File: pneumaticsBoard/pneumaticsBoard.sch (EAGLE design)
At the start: 51 parts, among them IC1 MAX232, Q1 60V/32A/35mΩ, Q2 60V/32A/35mΩ, Q3 60V/32A/35mΩ, Q4 60V/32A/35mΩ, Q5 60V/32A/35mΩ, Q6 60V/32A/35mΩ, Q7 60V/32A/35mΩ, Q8 60V/32A/35mΩ, U1 ATMEGA328P-PU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

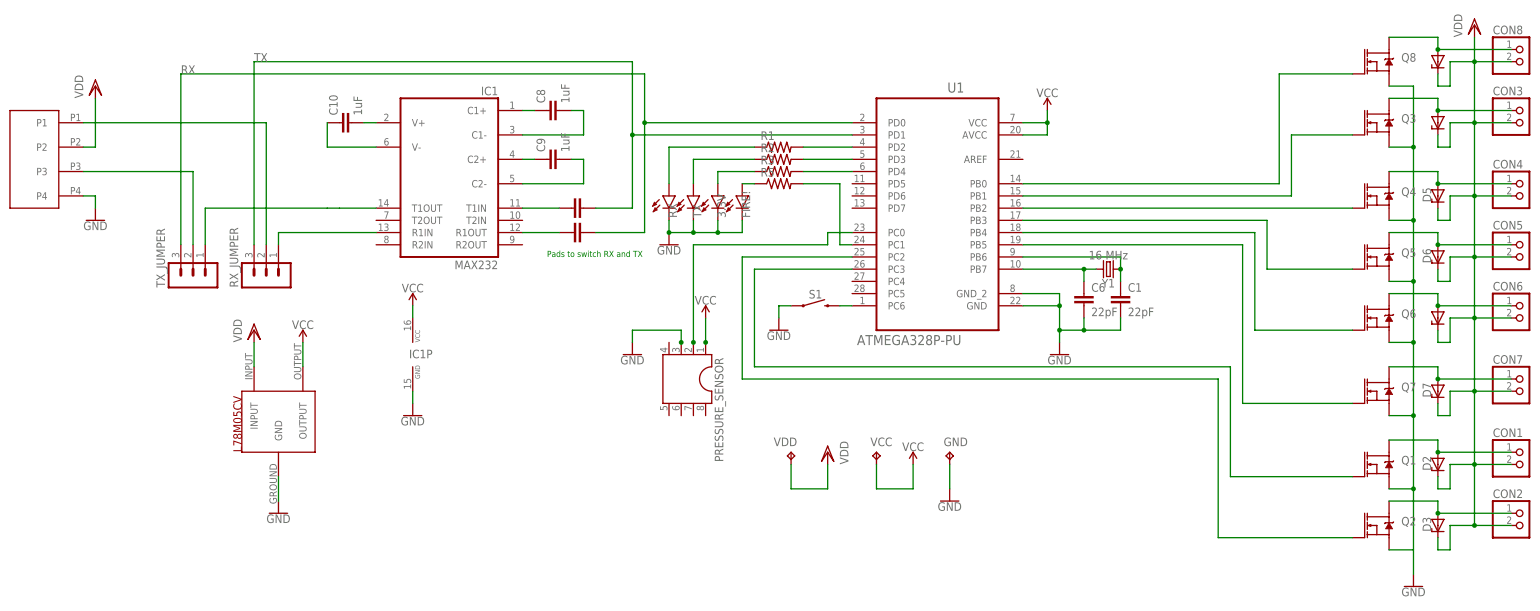
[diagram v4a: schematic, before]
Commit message: Changed regulator position, fixed traces
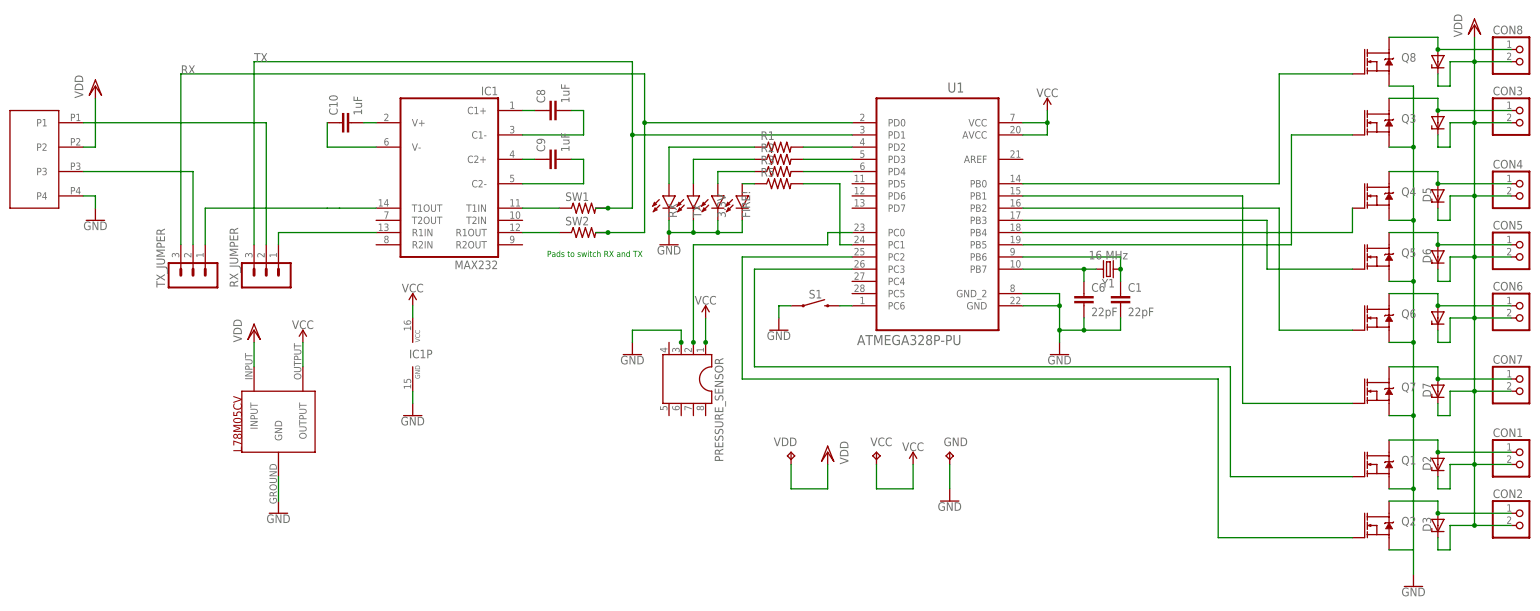
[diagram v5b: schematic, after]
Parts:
- removed C2, C3: 1uF, SparkFun-Capacitors:470PF-0603-50V-5%
- added SW1, SW2: (no value), resistor:R-US_0204/2V
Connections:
- removed net Q4: Q4.G, U1.PB2
- new net N$5: Q4.G, U1.PB4
- net N$17: now also SW1.1; no longer C2.1
- net N$18: now also SW2.1; no longer C3.1
- net Q3: now also U1.PB5; no longer U1.PB1
- net Q6: now also U1.PB2; no longer U1.PB4
- net Q7: now also U1.PB1; no longer U1.PB5
- net RX: now also SW2.2; no longer C3.2
- net TX: now also SW1.2; no longer C2.2
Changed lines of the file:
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@@
 <part name="TX_JUMPER" library="con-lstb" library_urn="urn:adsk.eagle:library:162" deviceset="MA03-1" device="" package3d_urn="urn:adsk.eagle:package:8339/1"/>
 <part name="RX_JUMPER" library="con-lstb" library_urn="urn:adsk.eagle:library:162" deviceset="MA03-1" device="" package3d_urn="urn:adsk.eagle:package:8339/1"/>
-<part name="C2" library="SparkFun-Capacitors" deviceset="470PF" device="-0603-50V-5%" value="1uF"/>
-<part name="C3" library="SparkFun-Capacitors" deviceset="470PF" device="-0603-50V-5%" value="1uF"/>
 <part name="Q1" library="SparkFun-DiscreteSemi" deviceset="MOSFET-NCH" device="-FQP30N06L" value="60V/32A/35mΩ"/>
 <part name="Q2" library="SparkFun-DiscreteSemi" deviceset="MOSFET-NCH" device="-FQP30N06L" value="60V/32A/35mΩ"/>
@@
 <part name="SUPPLY3" library="SparkFun-PowerSymbols" deviceset="VCC" device=""/>
 <part name="GND4" library="SparkFun-PowerSymbols" deviceset="GND" device=""/>
+<part name="SW2" library="resistor" library_urn="urn:adsk.eagle:library:348" deviceset="R-US_" device="0204/2V" package3d_urn="urn:adsk.eagle:package:25948/1"/>
+<part name="SW1" library="resistor" library_urn="urn:adsk.eagle:library:348" deviceset="R-US_" device="0204/2V" package3d_urn="urn:adsk.eagle:package:25948/1"/>
 </parts>
 <sheets>
@@
 <instance part="TX_JUMPER" gate="G$1" x="-137.16" y="25.4" rot="R90"/>
 <instance part="RX_JUMPER" gate="G$1" x="-121.92" y="25.4" rot="R90"/>
-<instance part="C2" gate="G$1" x="-55.88" y="40.64" smashed="yes" rot="R90"/>
-<instance part="C3" gate="G$1" x="-55.88" y="35.56" smashed="yes" rot="R90"/>
 <instance part="Q1" gate="NMOS" x="109.22" y="-12.7" smashed="yes">
 <attribute name="NAME" x="114.3" y="-12.7" size="1.778" layer="95" font="vector"/>
@@
 <instance part="SUPPLY3" gate="G$1" x="-114.3" y="12.7" rot="MR0"/>
 <instance part="GND4" gate="1" x="-119.38" y="-22.86"/>
+<instance part="SW2" gate="G$1" x="-55.88" y="35.56"/>
+<instance part="SW1" gate="G$1" x="-55.88" y="40.64"/>
 </instances>
 <busses>
@@
 <net name="Q3" class="0">
 <segment>
-<wire x1="91.44" y1="55.88" x2="91.44" y2="43.18" width="0.1524" layer="91"/>
+<wire x1="91.44" y1="55.88" x2="91.44" y2="33.02" width="0.1524" layer="91"/>
 <wire x1="104.14" y1="55.88" x2="91.44" y2="55.88" width="0.1524" layer="91"/>
-<pinref part="U1" gate="A" pin="PB1"/>
-<wire x1="91.44" y1="43.18" x2="35.56" y2="43.18" width="0.1524" layer="91"/>
 <pinref part="Q3" gate="NMOS" pin="G"/>
-</segment>
-</net>
-<net name="Q4" class="0">
-<segment>
-<wire x1="104.14" y1="40.64" x2="35.56" y2="40.64" width="0.1524" layer="91"/>
-<pinref part="U1" gate="A" pin="PB2"/>
-<pinref part="Q4" gate="NMOS" pin="G"/>
+<pinref part="U1" gate="A" pin="PB5"/>
+<wire x1="35.56" y1="33.02" x2="91.44" y2="33.02" width="0.1524" layer="91"/>
 </segment>
 </net>
@@
 <wire x1="86.36" y1="27.94" x2="86.36" y2="38.1" width="0.1524" layer="91"/>
 <wire x1="104.14" y1="27.94" x2="86.36" y2="27.94" width="0.1524" layer="91"/>
+<pinref part="Q5" gate="NMOS" pin="G"/>
 <pinref part="U1" gate="A" pin="PB3"/>
 <wire x1="35.56" y1="38.1" x2="86.36" y2="38.1" width="0.1524" layer="91"/>
-<pinref part="Q5" gate="NMOS" pin="G"/>
 </segment>
 </net>
@@
 <wire x1="-43.18" y1="58.42" x2="-43.18" y2="35.56" width="0.1524" layer="91"/>
 <pinref part="U1" gate="A" pin="PD0"/>
-<wire x1="-53.34" y1="35.56" x2="-43.18" y2="35.56" width="0.1524" layer="91"/>
+<wire x1="-53.34" y1="35.56" x2="-50.8" y2="35.56" width="0.1524" layer="91"/>
+<wire x1="-50.8" y1="35.56" x2="-43.18" y2="35.56" width="0.1524" layer="91"/>
 <wire x1="0" y1="58.42" x2="-43.18" y2="58.42" width="0.1524" layer="91"/>
 <wire x1="-43.18" y1="68.58" x2="-43.18" y2="58.42" width="0.1524" layer="91"/>
@@
 <wire x1="-43.18" y1="68.58" x2="-139.7" y2="68.58" width="0.1524" layer="91"/>
 <label x="-139.7" y="68.58" size="1.778" layer="95"/>
-<pinref part="C3" gate="G$1" pin="2"/>
+<pinref part="SW2" gate="G$1" pin="2"/>
+<junction x="-50.8" y="35.56"/>
 </segment>
 </net>
@@
 <net name="Q7" class="0">
 <segment>
-<pinref part="U1" gate="A" pin="PB5"/>
 <wire x1="104.14" y1="0" x2="81.28" y2="0" width="0.1524" layer="91"/>
-<wire x1="81.28" y1="0" x2="81.28" y2="33.02" width="0.1524" layer="91"/>
-<wire x1="35.56" y1="33.02" x2="81.28" y2="33.02" width="0.1524" layer="91"/>
+<wire x1="81.28" y1="0" x2="81.28" y2="43.18" width="0.1524" layer="91"/>
 <pinref part="Q7" gate="NMOS" pin="G"/>
+<pinref part="U1" gate="A" pin="PB1"/>
+<wire x1="81.28" y1="43.18" x2="35.56" y2="43.18" width="0.1524" layer="91"/>
 </segment>
 </net>
 <net name="Q6" class="0">
 <segment>
-<wire x1="83.82" y1="15.24" x2="104.14" y2="15.24" width="0.1524" layer="91"/>
-<pinref part="U1" gate="A" pin="PB4"/>
-<wire x1="83.82" y1="35.56" x2="35.56" y2="35.56" width="0.1524" layer="91"/>
-<wire x1="83.82" y1="15.24" x2="83.82" y2="35.56" width="0.1524" layer="91"/>
 <pinref part="Q6" gate="NMOS" pin="G"/>
+<pinref part="U1" gate="A" pin="PB2"/>
+<wire x1="88.9" y1="15.24" x2="104.14" y2="15.24" width="0.1524" layer="91"/>
+<wire x1="35.56" y1="40.64" x2="88.9" y2="40.64" width="0.1524" layer="91"/>
+<wire x1="88.9" y1="40.64" x2="88.9" y2="15.24" width="0.1524" layer="91"/>
 </segment>
 </net>
@@
 <segment>
 <wire x1="-45.72" y1="55.88" x2="-45.72" y2="40.64" width="0.1524" layer="91"/>
-<wire x1="-45.72" y1="40.64" x2="-53.34" y2="40.64" width="0.1524" layer="91"/>
+<wire x1="-45.72" y1="40.64" x2="-50.8" y2="40.64" width="0.1524" layer="91"/>
 <pinref part="U1" gate="A" pin="PD1"/>
+<wire x1="-50.8" y1="40.64" x2="-53.34" y2="40.64" width="0.1524" layer="91"/>
 <wire x1="0" y1="55.88" x2="-45.72" y2="55.88" width="0.1524" layer="91"/>
 <wire x1="-45.72" y1="55.88" x2="-45.72" y2="71.12" width="0.1524" layer="91"/>
@@
 <wire x1="-124.46" y1="33.02" x2="-124.46" y2="71.12" width="0.1524" layer="91"/>
 <label x="-124.46" y="71.12" size="1.778" layer="95"/>
-<pinref part="C2" gate="G$1" pin="2"/>
+<pinref part="SW1" gate="G$1" pin="2"/>
+<junction x="-50.8" y="40.64"/>
 </segment>
 </net>
@@
 <pinref part="IC1" gate="G$1" pin="T1IN"/>
 <wire x1="-60.96" y1="40.64" x2="-68.58" y2="40.64" width="0.1524" layer="91"/>
-<pinref part="C2" gate="G$1" pin="1"/>
+<pinref part="SW1" gate="G$1" pin="1"/>
 </segment>
 </net>
@@
 <pinref part="IC1" gate="G$1" pin="R1OUT"/>
 <wire x1="-68.58" y1="35.56" x2="-60.96" y2="35.56" width="0.1524" layer="91"/>
-<pinref part="C3" gate="G$1" pin="1"/>
-</segment>
-</net>
+<pinref part="SW2" gate="G$1" pin="1"/>
+</segment>
+</net>
+<net name="N$5" class="0">
+<segment>
+<pinref part="U1" gate="A" pin="PB4"/>
+<pinref part="Q4" gate="NMOS" pin="G"/>
+<wire x1="35.56" y1="35.56" x2="104.14" y2="35.56" width="0.1524" layer="91"/>
+<wire x1="104.14" y1="35.56" x2="104.14" y2="40.64" width="0.1524" layer="91"/>
+</segment>
+</net>
